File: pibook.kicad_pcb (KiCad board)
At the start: 2 copper layers, 85 x 85 mm, 161 parts, among them IC1 ATTINY48-A, J1 ComputeModule, J2 TRS_JACK_3PIN, P1 CONN_01X40, P2 USB_OTG, P3 CONN_01X02, P4 CONN_02X05, P5 USB_A, P6 CONN_02X06, P7 CONN_01X20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

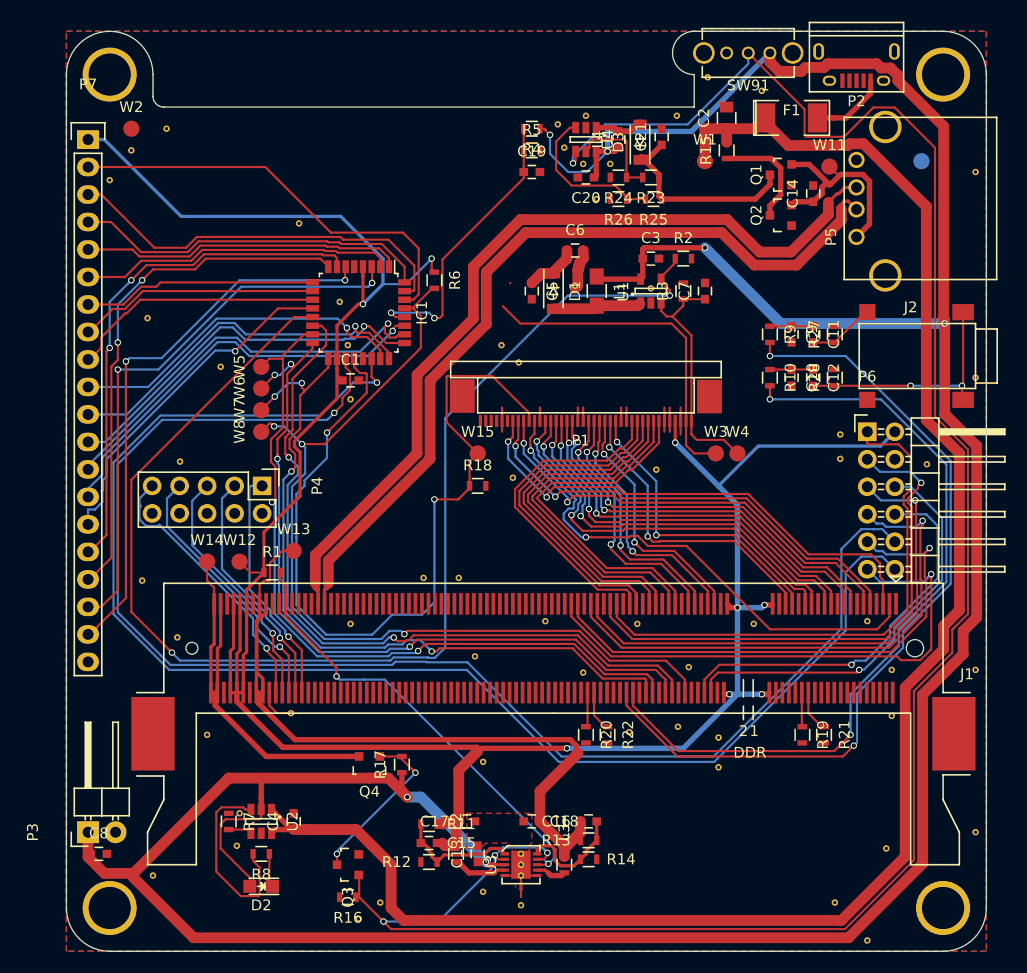
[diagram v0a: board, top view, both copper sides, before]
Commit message: fixed DRC, fixed component ref silkscreen
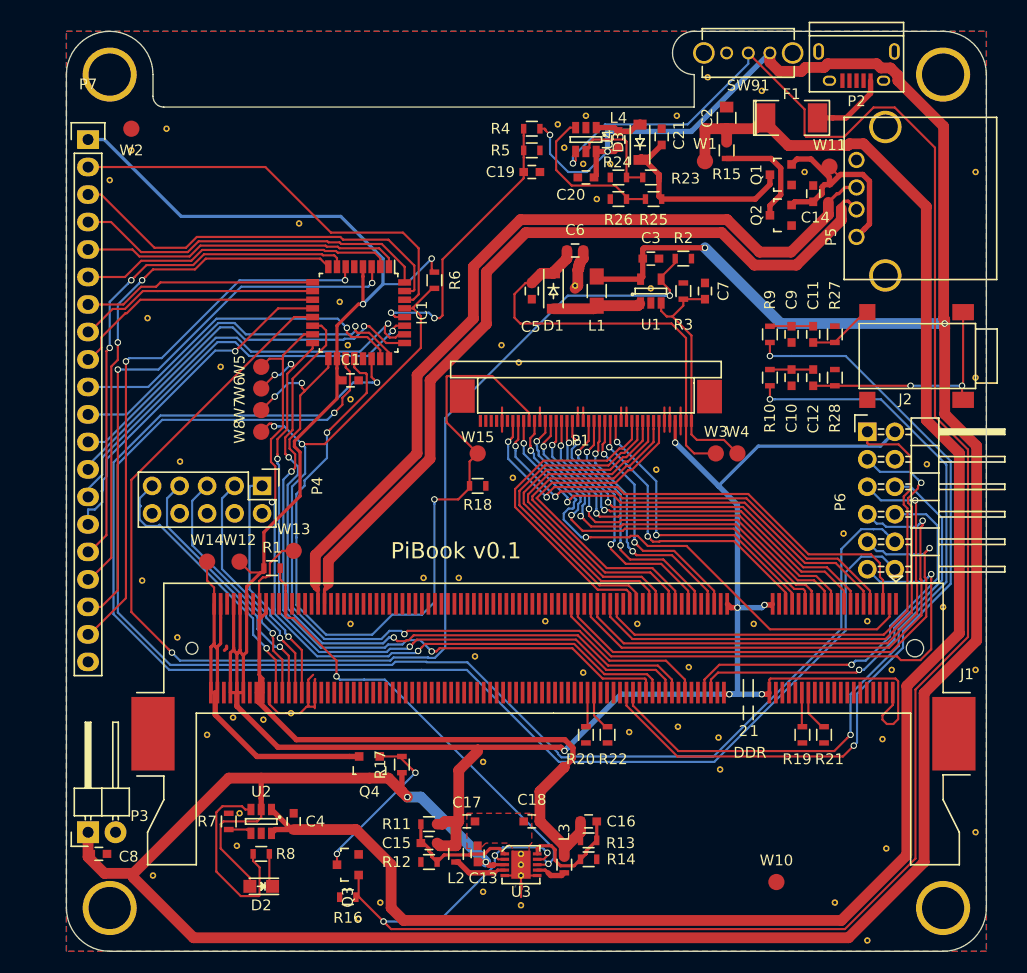
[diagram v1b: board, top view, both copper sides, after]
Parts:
- added REF**: VIA_0.6MM, ComputeModule:VIA_0.6MM, F.Cu at (141.2, 121.0)
- added REF**: VIA_0.6MM, ComputeModule:VIA_0.6MM, F.Cu at (91.2, 171.6)
- added REF**: VIA_0.6MM, ComputeModule:VIA_0.6MM, F.Cu at (88.4, 171.4)
- W10: moved to F.Cu
- moved W10 67.9 mm to (138.6, 186.6)
- moved REF** 16.7 mm to (154.0, 161.2)
- moved REF** 9.15 mm to (144.8, 154.4)
- moved REF** 2.31 mm to (148.4, 173.4)
- moved R1 0.40 mm to (92.0, 157.6)
- moved REF** 0.25 mm to (133.4, 176.2)
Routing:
- net +3V3: track 229.0 -> 253.7 mm
- net GND: track 23.6 -> 31.8 mm
- net /BACKL_A: track 36.1 -> 38.8 mm
- net +1V8: track 73.6 -> 72.4 mm
- net /CM_VBAT: track 37.9 -> 38.9 mm
- net +VUSB_OUT: track 20.3 -> 21.1 mm
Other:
- board text added: "PiBook v0.1"

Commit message: Fixed up some things for production (putting NPTH in same drill file, tidied up some silk screen)
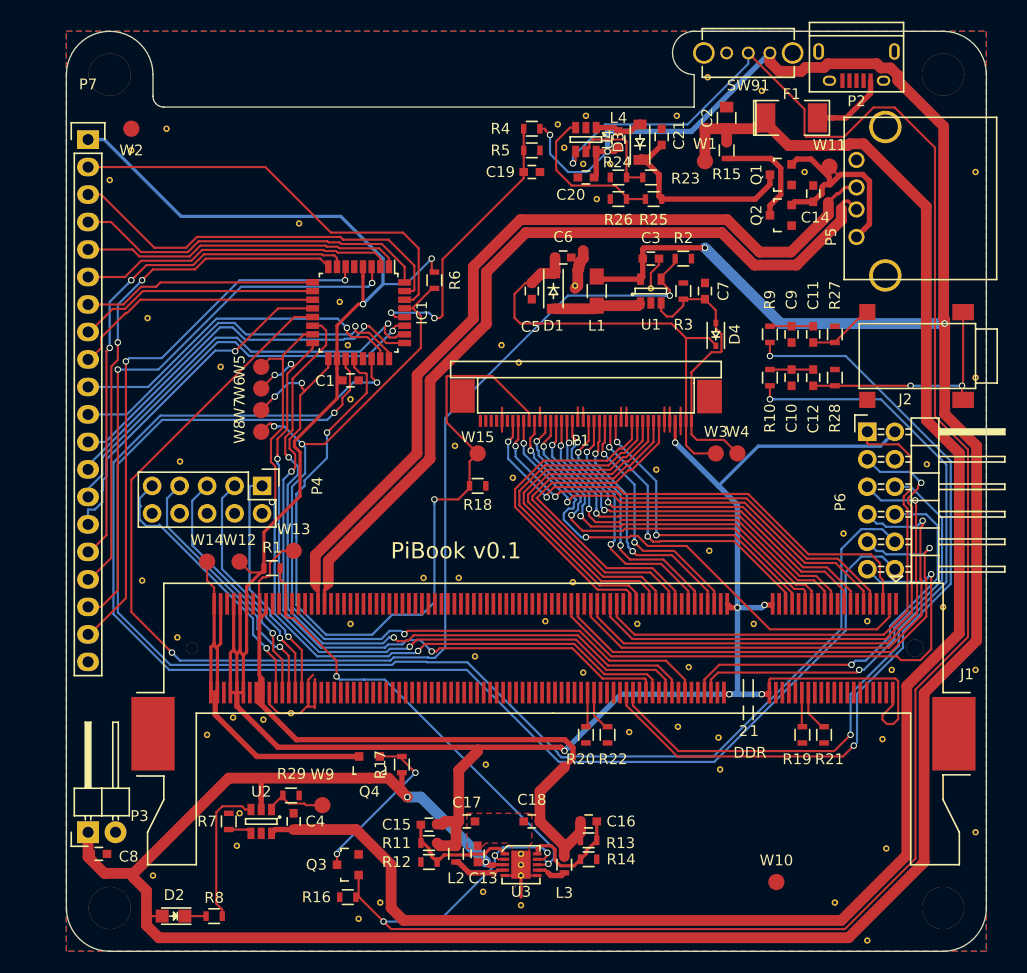
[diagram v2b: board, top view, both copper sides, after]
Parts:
- added D4: MM32Z24VT1G, Diodes_SMD:SOD-323, F.Cu at (133.0, 136.0)
- added R29: 10k, Resistors_SMD:R_0603, F.Cu at (93.8, 178.6)
- added REF**: VIA_0.6MM, ComputeModule:VIA_0.6MM, F.Cu at (132.4, 156.0)
- added REF**: VIA_0.6MM, ComputeModule:VIA_0.6MM, F.Cu at (119.8, 158.9)
- added REF**: VIA_0.6MM, ComputeModule:VIA_0.6MM, F.Cu at (108.9, 146.3)
- added W9: TS, Measurement_Points:Measurement_Point_Round-SMD-Pad_Small, F.Cu at (96.7, 179.5)
- J1: footprint Sockets:Socket_SODIMM_DDR1-2_TE_1612618 -> Socket_SODIMM_DDR1-2_TE_1612618
- moved D2 8.55 mm to (82.9, 189.8)
- moved R8 7.21 mm to (86.7, 189.8), turned to 0 degrees
- moved R11 1.75 mm to (106.5, 183.0)
- moved C15 1.70 mm to (106.5, 181.3)
- moved C6 1.28 mm to (118.9, 128.9)
- moved REF** 0.35 mm to (111.8, 175.8)
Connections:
- U2 pad 1: +VUSB_IN -> Net-(R29-Pad2)
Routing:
- net +BATT: track 307.7 -> 300.5 mm
- net Net-(R29-Pad2): track 0.00 -> 5.87 mm
- net Net-(R8-Pad2): track 18.1 -> 13.4 mm
- net /BACKL_K: track 22.6 -> 25.8 mm
- net GND: track 31.8 -> 34.8 mm
- net +VUSB_IN: track 162.1 -> 159.5 mm
- net /BACKL_A: track 38.8 -> 40.9 mm
- net Net-(D2-Pad1): track 3.12 -> 1.95 mm

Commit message: Fixed some DRCs
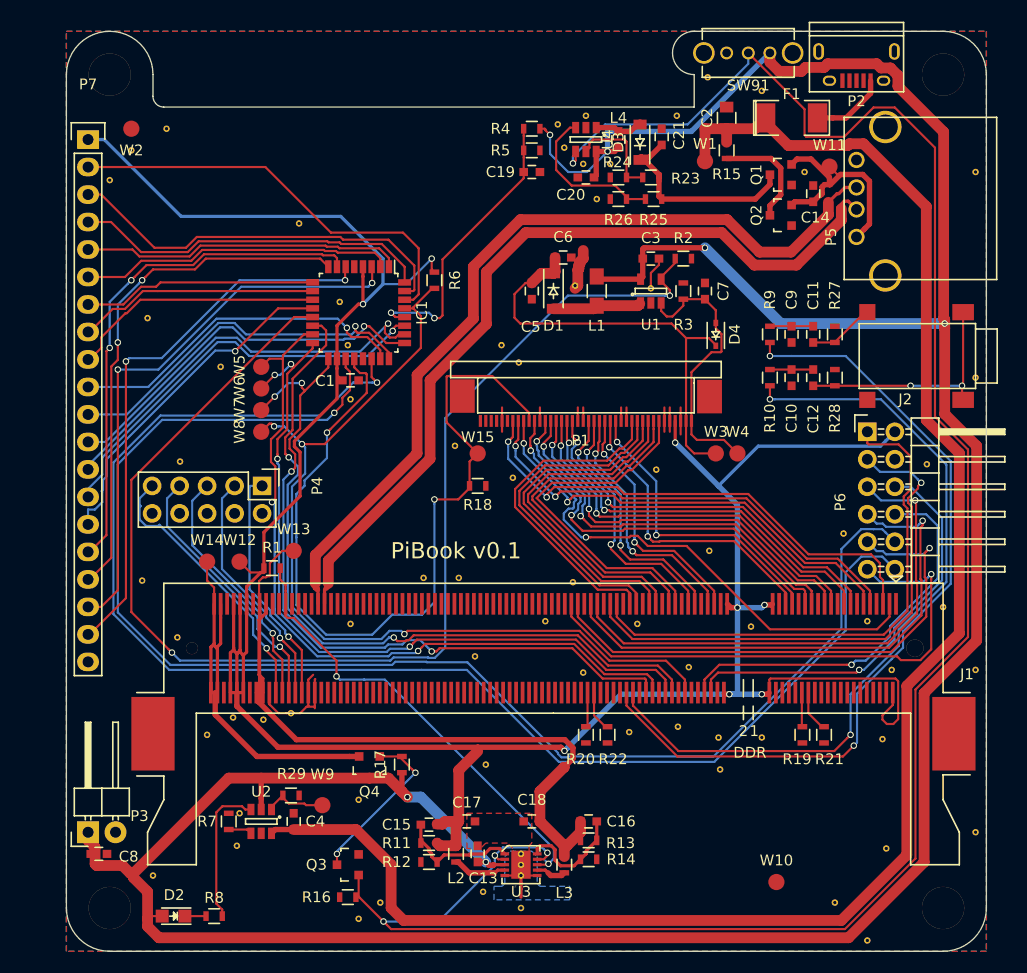
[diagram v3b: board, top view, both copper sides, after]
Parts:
- added REF**: VIA_0.6MM, ComputeModule:VIA_0.6MM, F.Cu at (100.0, 179.0)
- added REF**: VIA_0.6MM, ComputeModule:VIA_0.6MM, F.Cu at (137.2, 173.2)
- moved REF** 0.35 mm to (136.2, 163.0)
- moved REF** 0.25 mm to (115.0, 189.0)
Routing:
- added copper zone on B.Cu, net GNDPWR

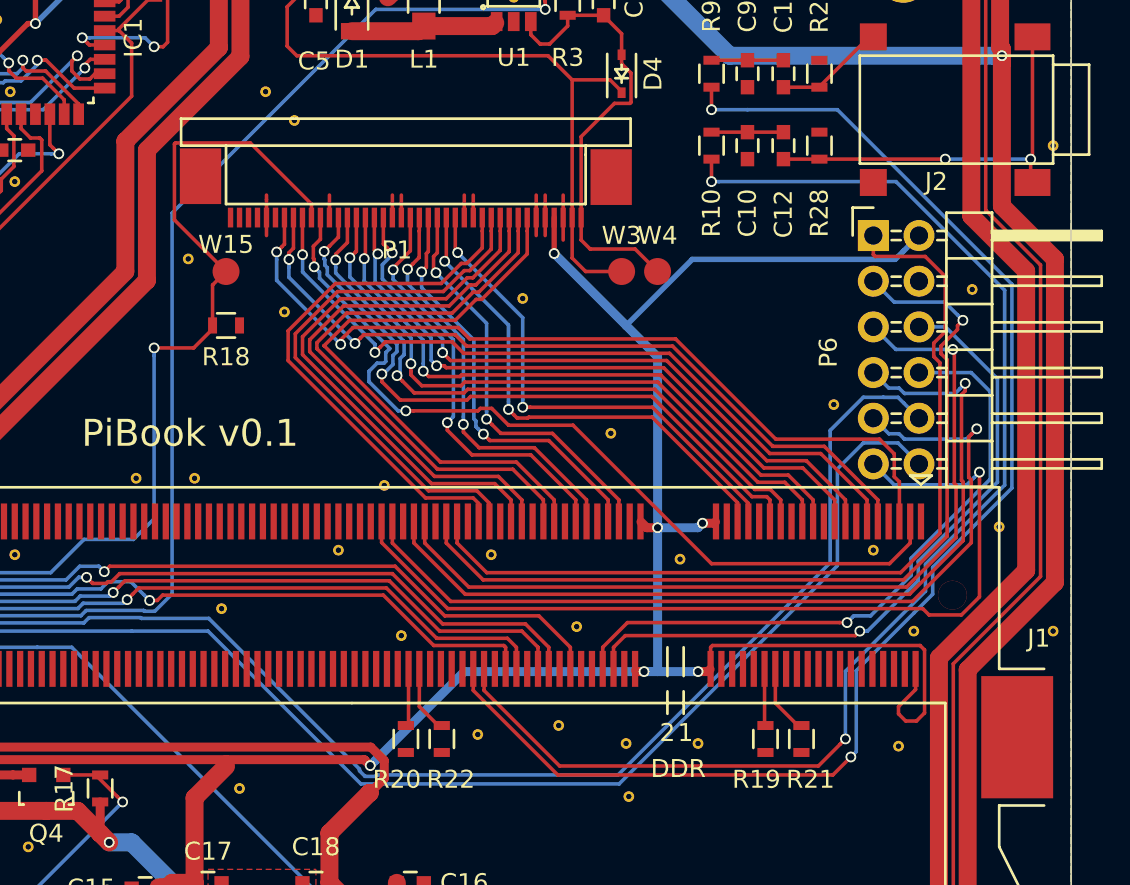
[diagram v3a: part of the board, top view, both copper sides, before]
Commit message: Fixed DRCs and some grounding on the SODIMM
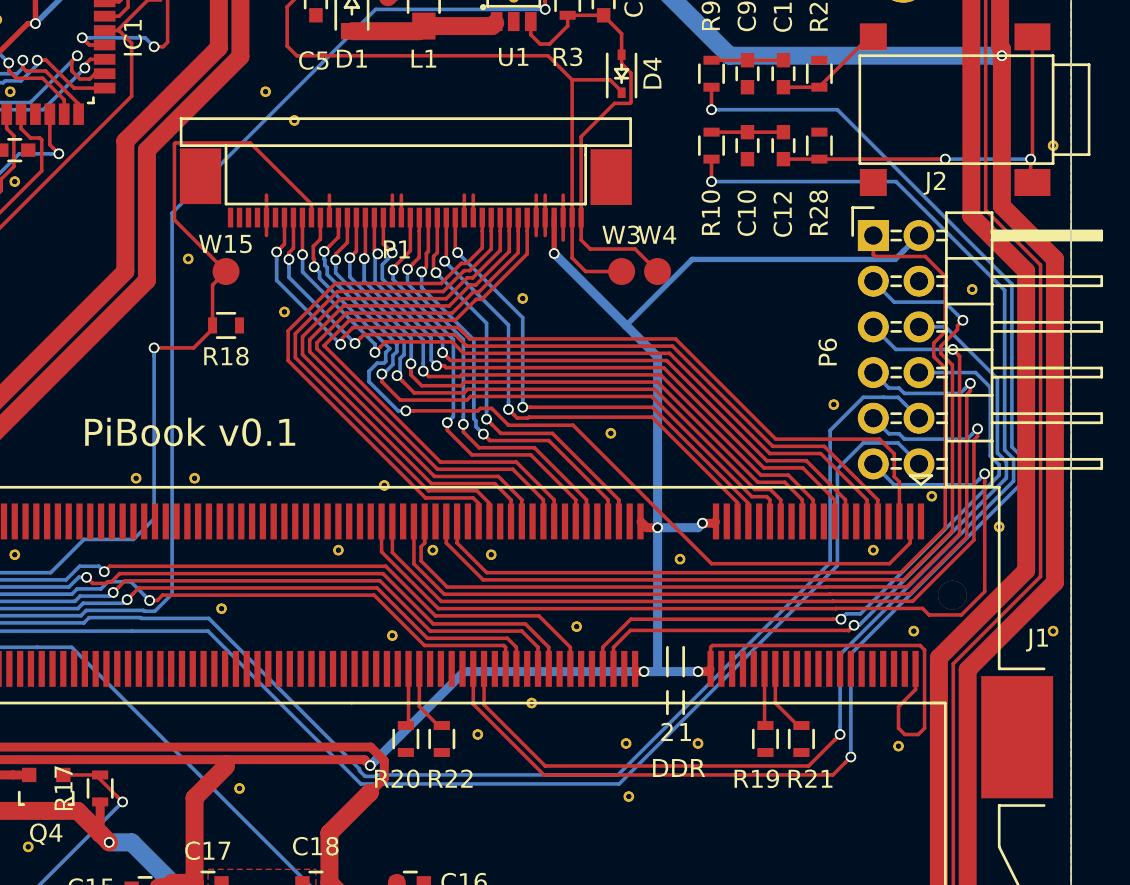
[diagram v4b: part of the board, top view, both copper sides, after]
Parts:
- added REF**: VIA_0.6MM, ComputeModule:VIA_0.6MM, F.Cu at (150.2, 159.5)
- added REF**: VIA_0.6MM, ComputeModule:VIA_0.6MM, F.Cu at (122.5, 162.5)
- moved REF** 1.95 mm to (128.0, 171.0)
- moved REF** 0.50 mm to (120.2, 167.2)
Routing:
- net +3V3: track 253.7 -> 255.3 mm
- net /USER_IO_2: track 48.4 -> 49.4 mm
- net /USER_IO_3: track 48.9 -> 49.9 mm
- net /AUDIO_R_PWM: track 76.5 -> 77.4 mm
- net /USER_IO_5: track 50.1 -> 50.7 mm
- net /AUDIO_L_PWM: track 72.3 -> 72.9 mm
